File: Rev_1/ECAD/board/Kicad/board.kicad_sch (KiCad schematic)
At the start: 1 part, among them U1 SD_CARD_READER

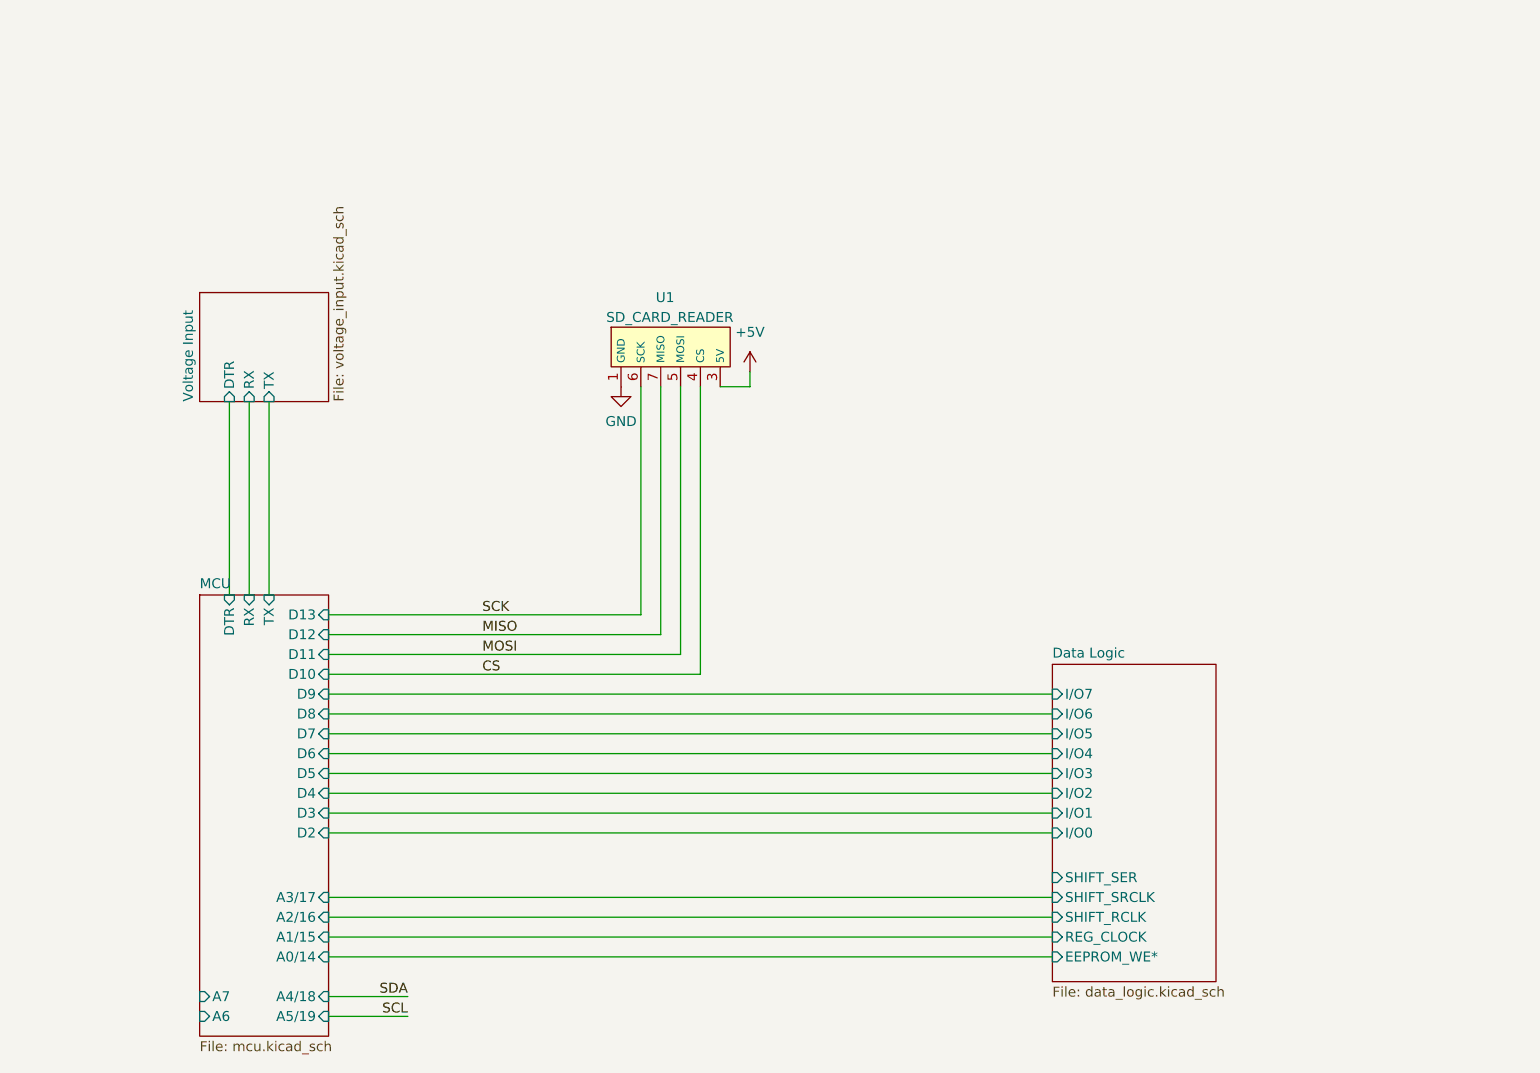
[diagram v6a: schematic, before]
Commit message: Removed I2C Display and added an SPI Display instead
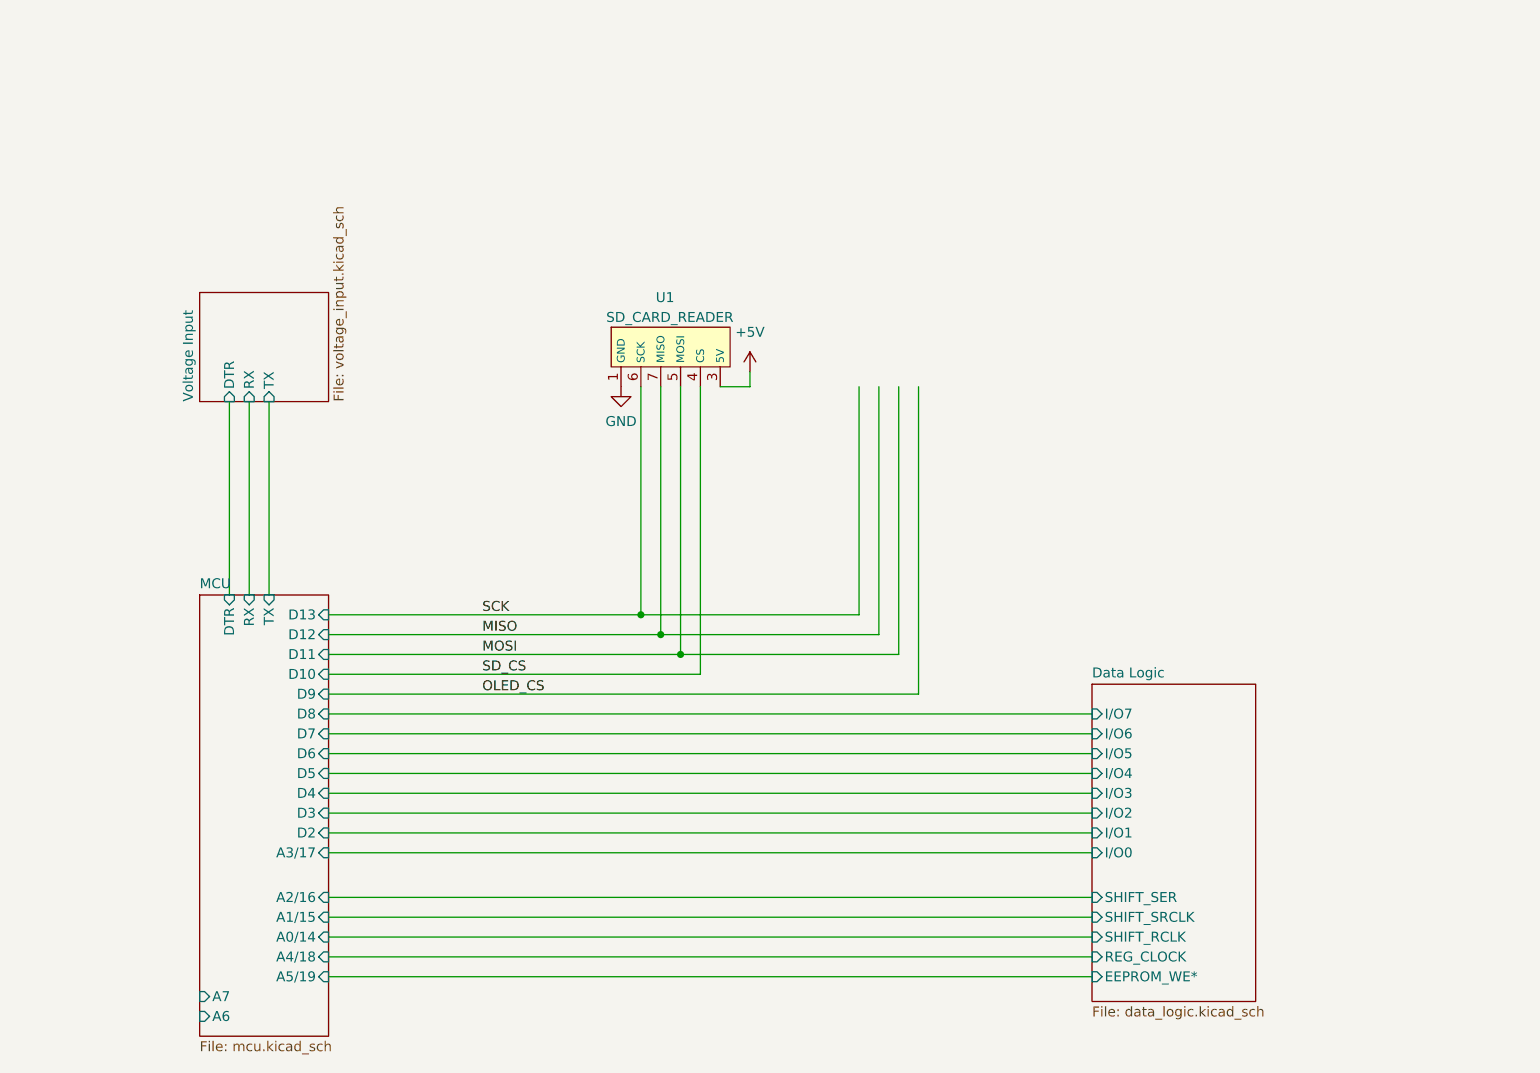
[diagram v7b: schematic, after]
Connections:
- net CS renamed SD_CS
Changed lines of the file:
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@@
     (rev "1")
   )
-  (wire (pts (xy 66.675 133.35) (xy 159.385 133.35))
-    (stroke (width 0) (type default))
-  )
-  (wire (pts (xy 159.385 114.935) (xy 66.675 114.935))
-    (stroke (width 0) (type default))
-  )
-  (wire (pts (xy 66.675 117.475) (xy 159.385 117.475))
+  (junction (at 106.68 94.615) (diameter 0) (color 0 0 0 0)
+  )
+  (junction (at 111.76 99.695) (diameter 0) (color 0 0 0 0)
+  )
+  (junction (at 109.22 97.155) (diameter 0) (color 0 0 0 0)
+  )
+  (wire (pts (xy 66.675 122.555) (xy 164.465 122.555))
+    (stroke (width 0) (type default))
+  )
+  (wire (pts (xy 139.7 99.695) (xy 111.76 99.695))
     (stroke (width 0) (type default))
   )
@@
     (stroke (width 0) (type default))
   )
-  (wire (pts (xy 159.385 120.015) (xy 66.675 120.015))
+  (wire (pts (xy 66.675 138.43) (xy 164.465 138.43))
+    (stroke (width 0) (type default))
+  )
+  (wire (pts (xy 66.675 107.315) (xy 164.465 107.315))
+    (stroke (width 0) (type default))
+  )
+  (wire (pts (xy 137.16 97.155) (xy 137.16 65.405))
     (stroke (width 0) (type default))
   )
@@
     (stroke (width 0) (type default))
   )
-  (wire (pts (xy 66.675 104.775) (xy 159.385 104.775))
+  (wire (pts (xy 66.675 117.475) (xy 164.465 117.475))
     (stroke (width 0) (type default))
   )
@@
     (stroke (width 0) (type default))
   )
-  (wire (pts (xy 159.385 122.555) (xy 66.675 122.555))
-    (stroke (width 0) (type default))
-  )
-  (wire (pts (xy 66.675 135.89) (xy 159.385 135.89))
+  (wire (pts (xy 66.675 109.855) (xy 164.465 109.855))
+    (stroke (width 0) (type default))
+  )
+  (wire (pts (xy 134.62 94.615) (xy 106.68 94.615))
     (stroke (width 0) (type default))
   )
@@
     (stroke (width 0) (type default))
   )
+  (wire (pts (xy 66.675 135.89) (xy 164.465 135.89))
+    (stroke (width 0) (type default))
+  )
   (wire (pts (xy 106.68 65.405) (xy 106.68 94.615))
     (stroke (width 0) (type default))
   )
+  (wire (pts (xy 66.675 112.395) (xy 164.465 112.395))
+    (stroke (width 0) (type default))
+  )
   (wire (pts (xy 116.84 65.405) (xy 120.65 65.405))
     (stroke (width 0) (type default))
   )
+  (wire (pts (xy 66.675 120.015) (xy 164.465 120.015))
+    (stroke (width 0) (type default))
+  )
   (wire (pts (xy 56.515 67.31) (xy 56.515 92.075))
     (stroke (width 0) (type default))
   )
+  (wire (pts (xy 66.675 130.81) (xy 164.465 130.81))
+    (stroke (width 0) (type default))
+  )
   (wire (pts (xy 114.3 102.235) (xy 114.3 65.405))
     (stroke (width 0) (type default))
   )
-  (wire (pts (xy 159.385 107.315) (xy 66.675 107.315))
-    (stroke (width 0) (type default))
-  )
-  (wire (pts (xy 66.675 138.43) (xy 159.385 138.43))
+  (wire (pts (xy 66.675 125.095) (xy 164.465 125.095))
+    (stroke (width 0) (type default))
+  )
+  (wire (pts (xy 66.675 104.775) (xy 142.24 104.775))
     (stroke (width 0) (type default))
   )
@@
     (stroke (width 0) (type default))
   )
+  (wire (pts (xy 66.675 114.935) (xy 164.465 114.935))
+    (stroke (width 0) (type default))
+  )
   (wire (pts (xy 66.675 97.155) (xy 109.22 97.155))
     (stroke (width 0) (type default))
   )
-  (wire (pts (xy 66.675 112.395) (xy 159.385 112.395))
-    (stroke (width 0) (type default))
-  )
-  (wire (pts (xy 66.675 143.51) (xy 76.835 143.51))
-    (stroke (width 0) (type default))
-  )
-  (wire (pts (xy 159.385 109.855) (xy 66.675 109.855))
-    (stroke (width 0) (type default))
-  )
-  (wire (pts (xy 66.675 130.81) (xy 159.385 130.81))
-    (stroke (width 0) (type default))
-  )
-  (wire (pts (xy 66.675 146.05) (xy 76.835 146.05))
+  (wire (pts (xy 137.16 97.155) (xy 109.22 97.155))
+    (stroke (width 0) (type default))
+  )
+  (wire (pts (xy 142.24 65.405) (xy 142.24 104.775))
+    (stroke (width 0) (type default))
+  )
+  (wire (pts (xy 66.675 140.97) (xy 164.465 140.97))
+    (stroke (width 0) (type default))
+  )
+  (wire (pts (xy 134.62 65.405) (xy 134.62 94.615))
+    (stroke (width 0) (type default))
+  )
+  (wire (pts (xy 139.7 65.405) (xy 139.7 99.695))
+    (stroke (width 0) (type default))
+  )
+  (wire (pts (xy 66.675 133.35) (xy 164.465 133.35))
     (stroke (width 0) (type default))
   )
@@
     (effects (font (size 1.27 1.27)) (justify left bottom))
   )
-  (label "SDA" (at 76.835 143.51 180) (fields_autoplaced)
-    (effects (font (size 1.27 1.27)) (justify right bottom))
-  )
-  (label "CS" (at 86.36 102.235 0) (fields_autoplaced)
+  (label "SD_CS" (at 86.36 102.235 0) (fields_autoplaced)
     (effects (font (size 1.27 1.27)) (justify left bottom))
   )
@@
     (effects (font (size 1.27 1.27)) (justify left bottom))
   )
-  (label "SCL" (at 76.835 146.05 180) (fields_autoplaced)
-    (effects (font (size 1.27 1.27)) (justify right bottom))
+  (label "OLED_CS" (at 86.36 104.775 0) (fields_autoplaced)
+    (effects (font (size 1.27 1.27)) (justify left bottom))
   )
   (symbol (lib_id "power:GND") (at 104.14 65.405 0) (unit 1)
@@
     )
   )
-  (sheet (at 159.385 100.965) (size 20.955 40.64) (fields_autoplaced)
+  (sheet (at 164.465 103.505) (size 20.955 40.64) (fields_autoplaced)
     (stroke (width 0.1524) (type solid))
     (fill (color 0 0 0 0.0000))
-    (property "Sheetname" "Data Logic" (at 159.385 100.2534 0)
+    (property "Sheetname" "Data Logic" (at 164.465 102.7934 0)
       (effects (font (size 1.27 1.27)) (justify left bottom))
     )
-    (property "Sheetfile" "data_logic.kicad_sch" (at 159.385 142.1896 0)
+    (property "Sheetfile" "data_logic.kicad_sch" (at 164.465 144.7296 0)
       (effects (font (size 1.27 1.27)) (justify left top))
     )
-    (pin "I{slash}O0" input (at 159.385 122.555 180)
-      (effects (font (size 1.27 1.27)) (justify left))
-    )
-    (pin "I{slash}O2" input (at 159.385 117.475 180)
-      (effects (font (size 1.27 1.27)) (justify left))
-    )
-    (pin "I{slash}O1" input (at 159.385 120.015 180)
-      (effects (font (size 1.27 1.27)) (justify left))
-    )
-    (pin "I{slash}O3" input (at 159.385 114.935 180)
-      (effects (font (size 1.27 1.27)) (justify left))
-    )
-    (pin "I{slash}O4" input (at 159.385 112.395 180)
-      (effects (font (size 1.27 1.27)) (justify left))
-    )
-    (pin "I{slash}O6" input (at 159.385 107.315 180)
-      (effects (font (size 1.27 1.27)) (justify left))
-    )
-    (pin "I{slash}O7" input (at 159.385 104.775 180)
-      (effects (font (size 1.27 1.27)) (justify left))
-    )
-    (pin "I{slash}O5" input (at 159.385 109.855 180)
-      (effects (font (size 1.27 1.27)) (justify left))
-    )
-    (pin "REG_CLOCK" input (at 159.385 135.89 180)
-      (effects (font (size 1.27 1.27)) (justify left))
-    )
-    (pin "EEPROM_WE*" input (at 159.385 138.43 180)
-      (effects (font (size 1.27 1.27)) (justify left))
-    )
-    (pin "SHIFT_SER" input (at 159.385 128.27 180)
-      (effects (font (size 1.27 1.27)) (justify left))
-    )
-    (pin "SHIFT_SRCLK" input (at 159.385 130.81 180)
-      (effects (font (size 1.27 1.27)) (justify left))
-    )
-    (pin "SHIFT_RCLK" input (at 159.385 133.35 180)
+    (pin "I{slash}O0" input (at 164.465 125.095 180)
+      (effects (font (size 1.27 1.27)) (justify left))
+    )
+    (pin "I{slash}O2" input (at 164.465 120.015 180)
+      (effects (font (size 1.27 1.27)) (justify left))
+    )
+    (pin "I{slash}O1" input (at 164.465 122.555 180)
+      (effects (font (size 1.27 1.27)) (justify left))
+    )
+    (pin "I{slash}O3" input (at 164.465 117.475 180)
+      (effects (font (size 1.27 1.27)) (justify left))
+    )
+    (pin "I{slash}O4" input (at 164.465 114.935 180)
+      (effects (font (size 1.27 1.27)) (justify left))
+    )
+    (pin "I{slash}O6" input (at 164.465 109.855 180)
+      (effects (font (size 1.27 1.27)) (justify left))
+    )
+    (pin "I{slash}O7" input (at 164.465 107.315 180)
+      (effects (font (size 1.27 1.27)) (justify left))
+    )
+    (pin "I{slash}O5" input (at 164.465 112.395 180)
+      (effects (font (size 1.27 1.27)) (justify left))
+    )
+    (pin "REG_CLOCK" input (at 164.465 138.43 180)
+      (effects (font (size 1.27 1.27)) (justify left))
+    )
+    (pin "EEPROM_WE*" input (at 164.465 140.97 180)
+      (effects (font (size 1.27 1.27)) (justify left))
+    )
+    (pin "SHIFT_SER" input (at 164.465 130.81 180)
+      (effects (font (size 1.27 1.27)) (justify left))
+    )
+    (pin "SHIFT_SRCLK" input (at 164.465 133.35 180)
+      (effects (font (size 1.27 1.27)) (justify left))
+    )
+    (pin "SHIFT_RCLK" input (at 164.465 135.89 180)
       (effects (font (size 1.27 1.27)) (justify left))
     )
@@
       (effects (font (size 1.27 1.27)) (justify right))
     )
-    (pin "A5{slash}19" input (at 66.675 146.05 0)
-      (effects (font (size 1.27 1.27)) (justify right))
-    )
-    (pin "A4{slash}18" input (at 66.675 143.51 0)
-      (effects (font (size 1.27 1.27)) (justify right))
-    )
-    (pin "A3{slash}17" input (at 66.675 130.81 0)
+    (pin "A5{slash}19" input (at 66.675 140.97 0)
+      (effects (font (size 1.27 1.27)) (justify right))
+    )
+    (pin "A4{slash}18" input (at 66.675 138.43 0)
+      (effects (font (size 1.27 1.27)) (justify right))
+    )
+    (pin "A3{slash}17" input (at 66.675 125.095 0)
       (effects (font (size 1.27 1.27)) (justify right))
     )
@@
       (effects (font (size 1.27 1.27)) (justify left))
     )
-    (pin "A1{slash}15" input (at 66.675 135.89 0)
-      (effects (font (size 1.27 1.27)) (justify right))
-    )
-    (pin "A2{slash}16" input (at 66.675 133.35 0)
-      (effects (font (size 1.27 1.27)) (justify right))
-    )
-    (pin "A0{slash}14" input (at 66.675 138.43 0)
-      (effects (font (size 1.27 1.27)) (justify right))
-    )
+    (pin "A1{slash}15" input (at 66.675 133.35 0)
+      (effects (font (size 1.27 1.27)) (justify right))
+    )
+    (pin "A2{slash}16" input (at 66.675 130.81 0)
+      (effects (font (size 1.27 1.27)) (justify right))
+    )
+    (pin "A0{slash}14" input (at 66.675 135.89 0)
+      (effects (font (size 1.27 1.27)) (justify right))
+    )

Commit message: Changed from 4-bit registers to shift registers
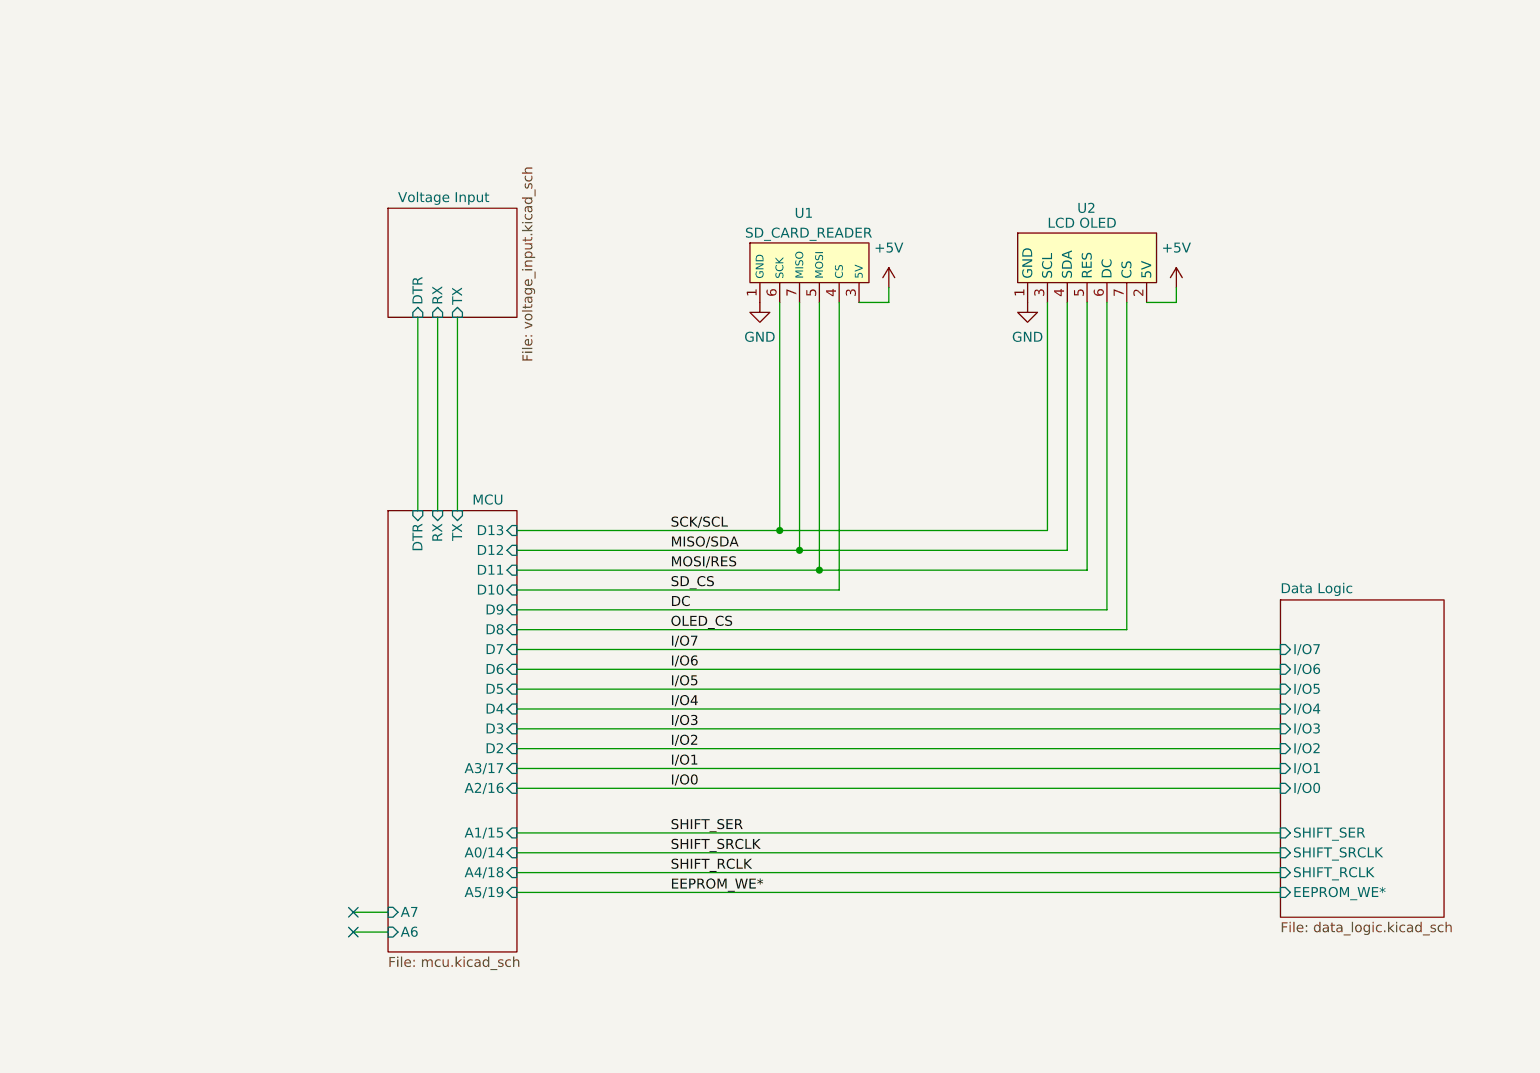
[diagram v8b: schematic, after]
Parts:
- added U2: LCD OLED, EEPROM_PROGRAMMER:LCD_OLED, symbol EEPROM_PROGRAMMER:LCD_OLED
- U1: footprint (none) -> EEPROM_PROGRAMMER:SD_CARD_READER
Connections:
- net +5V: now also U2.2 (5V)
- net GND: now also U2.1 (GND)
- net OLED_CS: now also U2.7 (CS)
- net MISO renamed MISO/SDA
- net MISO/SDA: now also U2.4 (SDA)
- net MOSI renamed MOSI/RES
- net MOSI/RES: now also U2.5 (RES)
- net SCK renamed SCK/SCL
- net SCK/SCL: now also U2.3 (SCL)
- new net DC: U2.6 (DC)
- no-connect marks 0 -> 2
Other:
- sheet Data Logic ports: added none; removed REG_CLOCK
- moved on the sheet: U1
